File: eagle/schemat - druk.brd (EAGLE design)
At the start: 210 parts, among them IC1 MEGA8-AI, IC2 MEGA8-AI, IC3 MEGA8-AI, IC4 MEGA8-AI, IC5 MEGA8-AI, IC6 MEGA8-AI, Q1 N-MOSFET BSS138, Q10 N-MOSFET BSS138, Q11 N-MOSFET BSS138, Q12 N-MOSFET BSS138, Q2 N-MOSFET BSS138, Q3 N-MOSFET BSS138, Q4 N-MOSFET BSS138, Q5 N-MOSFET BSS138, Q6 N-MOSFET BSS138, Q7 N-MOSFET BSS138, Q8 N-MOSFET BSS138, Q9 N-MOSFET BSS138, U1 LCD-16X2SILK, U2 LCD-16X2SILK, U3 LCD-16X2SILK, U4 LCD-16X2SILK, U5 LCD-16X2SILK, U6 LCD-16X2SILK, Y1 16MHz, Y2 16MHz, Y3 16MHz, Y4 16MHz, Y5 16MHz, Y6 16MHz

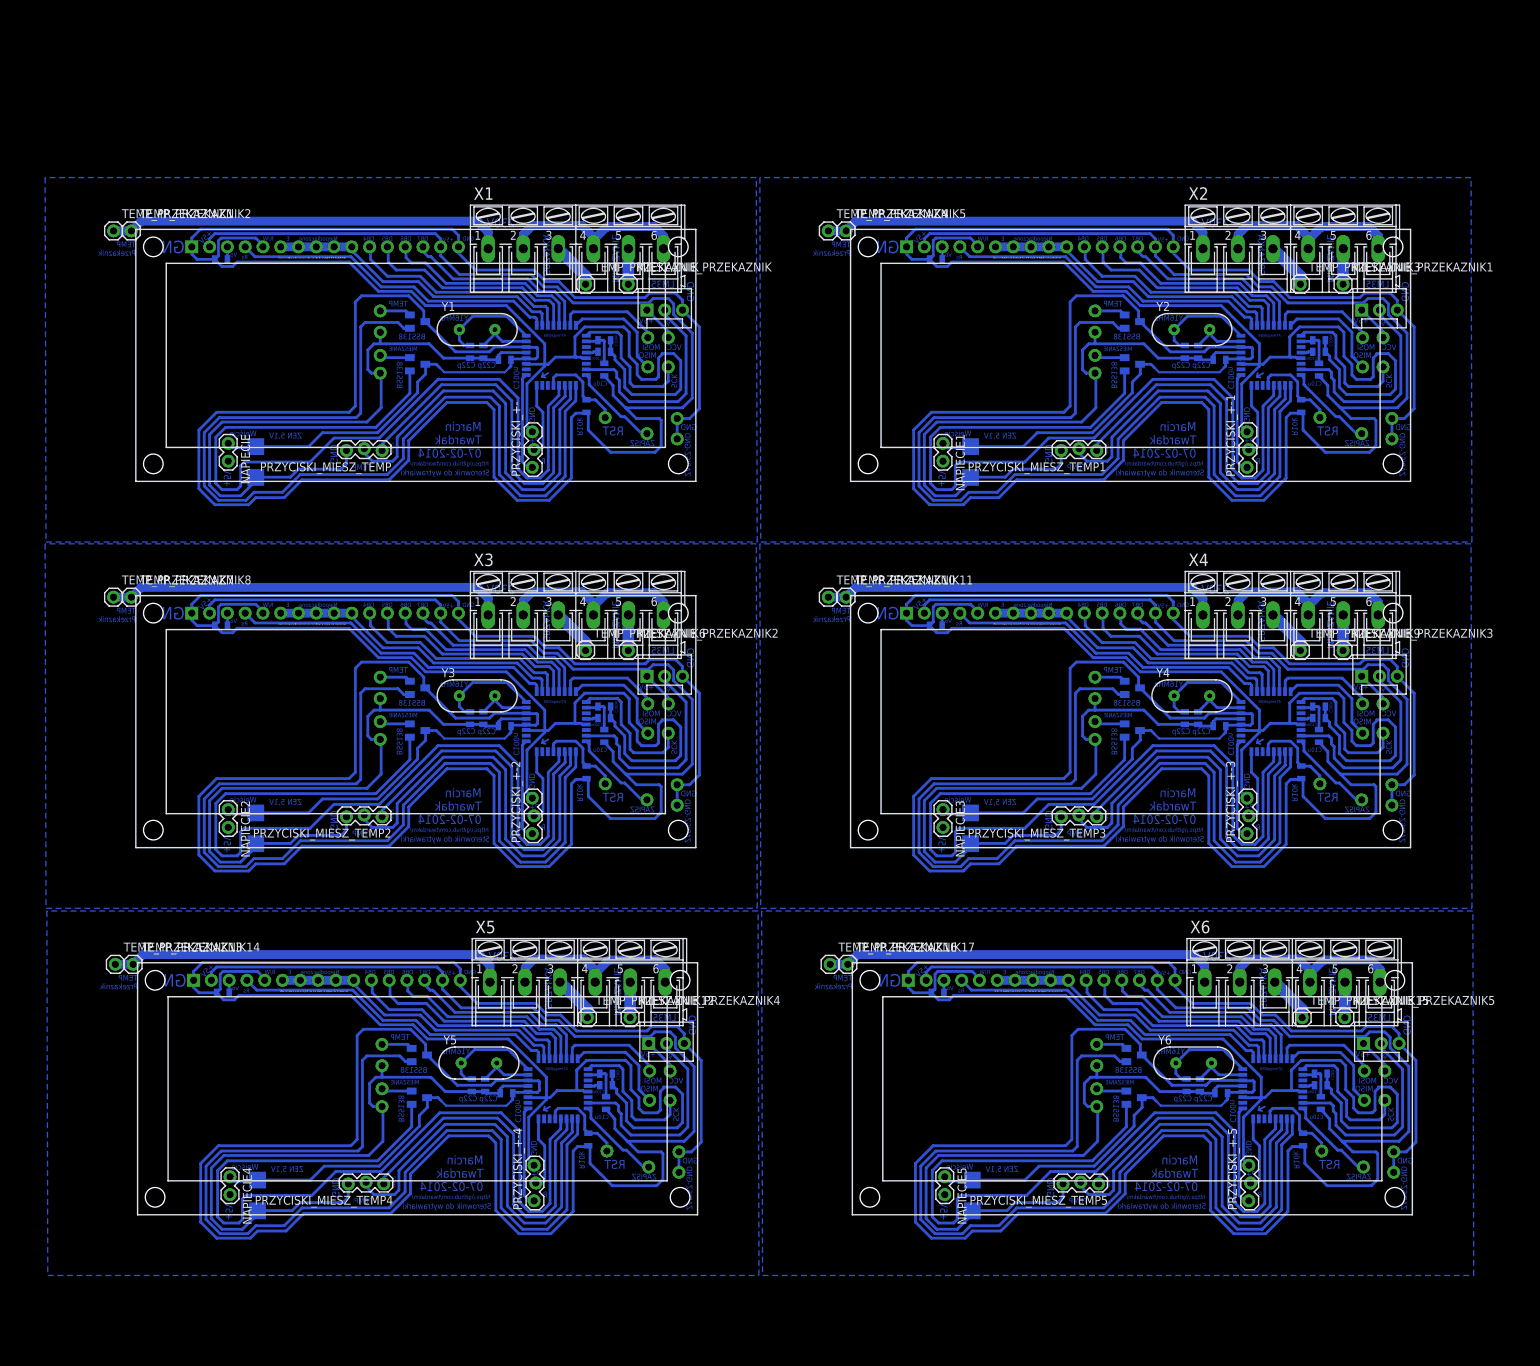
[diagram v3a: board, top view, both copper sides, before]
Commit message: Zmieniony schemat + zmiany w programie
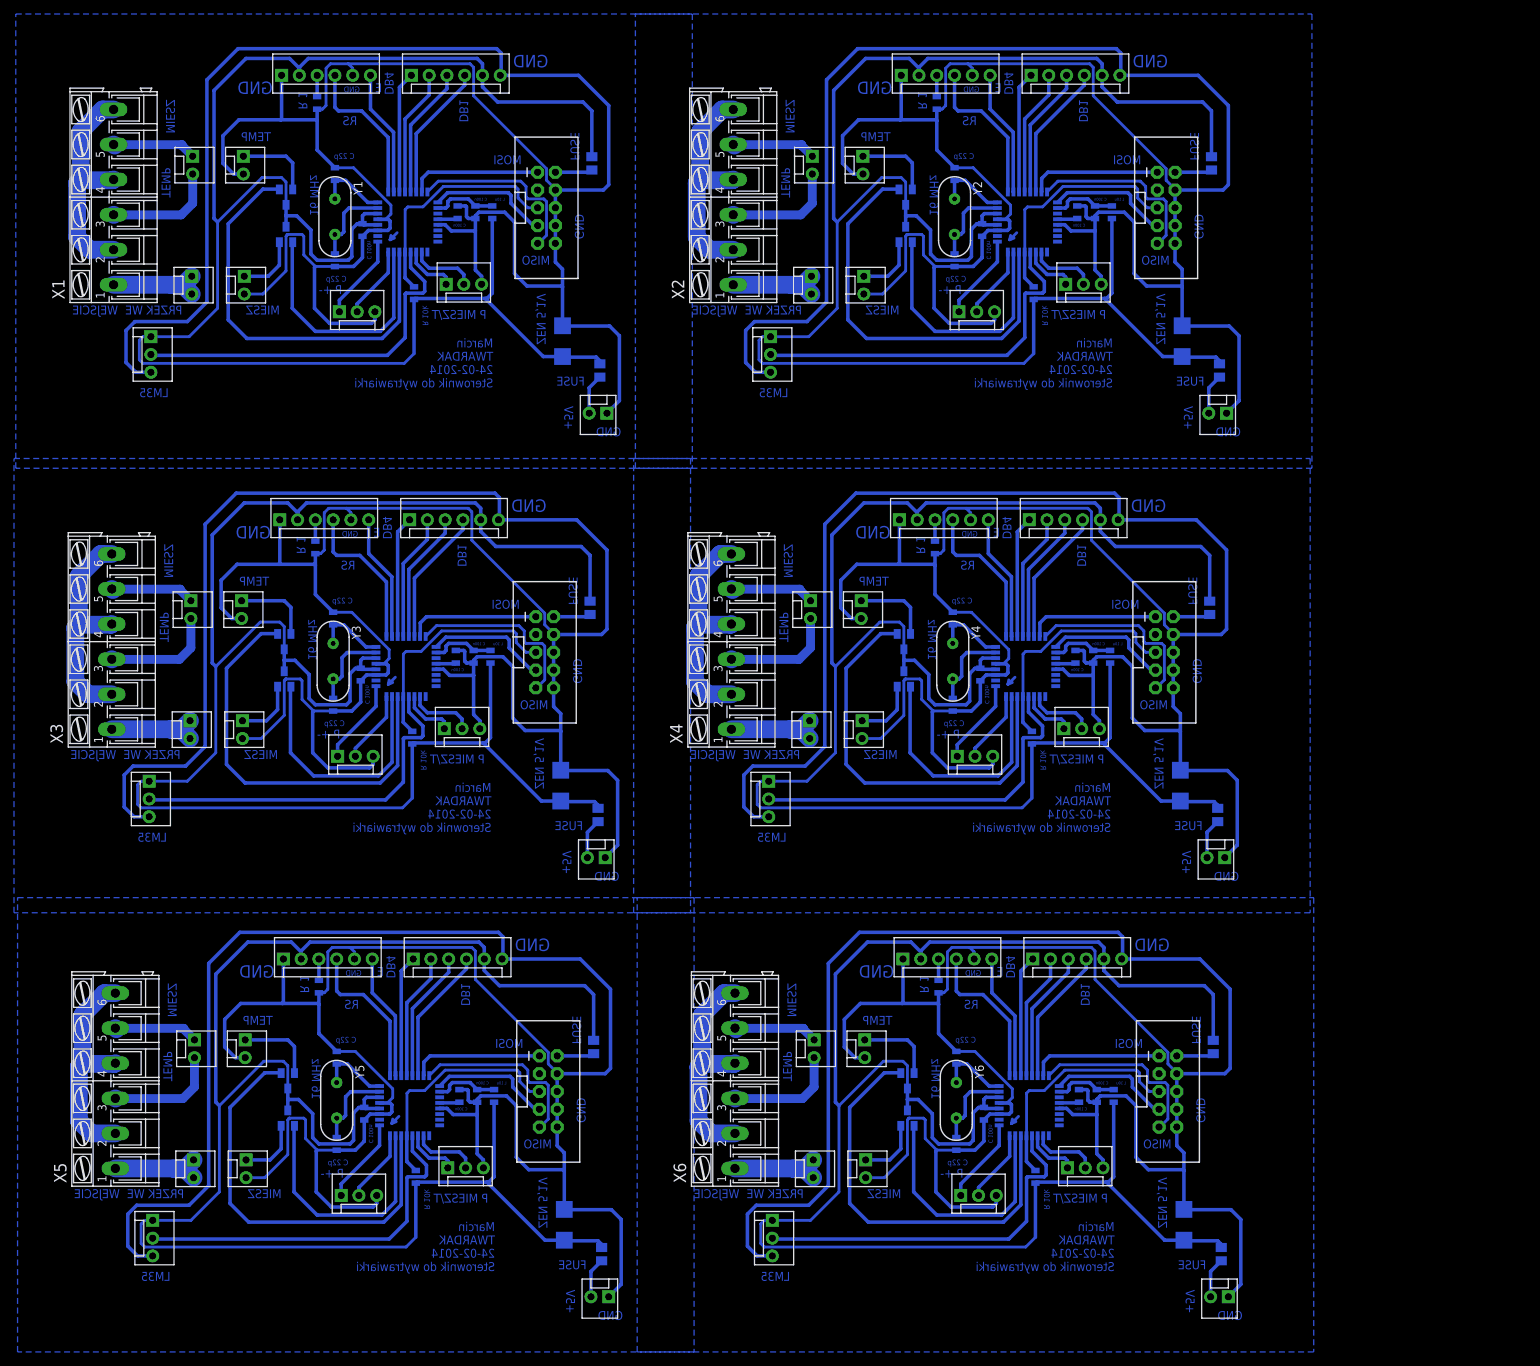
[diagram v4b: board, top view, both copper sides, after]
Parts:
- removed GND, GND1, GND2, GND3, GND4, GND5, MIESZANIE_GND, MIESZANIE_GND1, MIESZANIE_GND2, MIESZANIE_GND3, MIESZANIE_GND4, MIESZANIE_GND5, MISO, MISO1, MISO2, MISO3, MISO4, MISO5, MOSI, MOSI1, MOSI2, MOSI3, MOSI4, MOSI5, RESET, RESET1, RESET2, RESET3, RESET4, RESET5, SCK, SCK1, SCK2, SCK3, SCK4, SCK5, TEMP_GND, TEMP_GND1, TEMP_GND2, TEMP_GND3, TEMP_GND4, TEMP_GND5, VCC, VCC1, VCC2, VCC3, VCC4, VCC5, ZAPISZ, ZAPISZ1, ZAPISZ2, ZAPISZ3, ZAPISZ4, ZAPISZ5, ZAPISZ_GND, ZAPISZ_GND1, ZAPISZ_GND2, ZAPISZ_GND3, ZAPISZ_GND4, ZAPISZ_GND5: M01NOSILK-KIT, SparkFun-Connectors:1X01NS-KIT
- removed MIESZANIE_PRZEKAZNIK, MIESZANIE_PRZEKAZNIK1, MIESZANIE_PRZEKAZNIK2, MIESZANIE_PRZEKAZNIK3, MIESZANIE_PRZEKAZNIK4, MIESZANIE_PRZEKAZNIK5, TEMP_PRZEKAZNIK10, TEMP_PRZEKAZNIK11, TEMP_PRZEKAZNIK12, TEMP_PRZEKAZNIK13, TEMP_PRZEKAZNIK14, TEMP_PRZEKAZNIK15, TEMP_PRZEKAZNIK16, TEMP_PRZEKAZNIK17, TEMP_PRZEKAZNIK6, TEMP_PRZEKAZNIK7, TEMP_PRZEKAZNIK8, TEMP_PRZEKAZNIK9: M01PTH, SparkFun-Connectors:1X01
- removed U1, U2, U3, U4, U5, U6: LCD-16X2SILK, SparkFun-Displays:LCD-16X2
- added LCD1, LCD10, LCD11, LCD12, LCD2, LCD3, LCD4, LCD5, LCD6, LCD7, LCD8, LCD9: (no value), SparkFun-Connectors:MOLEX-1X6
- added PRZEKAZNIK_NAPIECIE, PRZEKAZNIK_NAPIECIE1, PRZEKAZNIK_NAPIECIE2, PRZEKAZNIK_NAPIECIE3, PRZEKAZNIK_NAPIECIE4, PRZEKAZNIK_NAPIECIE5: M02POLAR, SparkFun-Connectors:MOLEX-1X2
- added R13, R17, R21: 10k, SparkFun-Passives:0805
- added R14, R15, R18, R19, R22, R23: FUSE 500mA, resistor:M0805
- added R16, R20, R24: 1, SparkFun-Passives:0805
- added U$10, U$12, U$8: AVR_SPI_PROG2PTH2, SparkFun-Connectors:2X5-SHROUDED
- added U$11, U$7, U$9: ZENER 5V, SparkFun-DiscreteSemi:SMB-DIODE
- MIESZANIE, MIESZANIE1, MIESZANIE2, MIESZANIE3, MIESZANIE4, MIESZANIE5, TEMP, TEMP1, TEMP2, TEMP3, TEMP4, TEMP5: value M01NOSILK-KIT -> M02POLAR; device SparkFun-Connectors:1X01NS-KIT -> SparkFun-Connectors:MOLEX-1X2
- NAPIECIE, NAPIECIE1, NAPIECIE2, NAPIECIE3, NAPIECIE4, NAPIECIE5: value M02PTH -> M02POLAR; device SparkFun-Connectors:1X02 -> SparkFun-Connectors:MOLEX-1X2
- PRZYCISKI_+-, PRZYCISKI_+-1, PRZYCISKI_+-2, PRZYCISKI_+-3, PRZYCISKI_+-4, PRZYCISKI_+-5, PRZYCISKI_MIESZ_TEMP, PRZYCISKI_MIESZ_TEMP1, PRZYCISKI_MIESZ_TEMP2, PRZYCISKI_MIESZ_TEMP3, PRZYCISKI_MIESZ_TEMP4, PRZYCISKI_MIESZ_TEMP5: device SparkFun-Connectors:1X03_LOCK -> SparkFun-Connectors:MOLEX-1X3
- R10, R4, R6: value 1 -> FUSE 500mA; device SparkFun-Passives:0805 -> resistor:M0805
- R11, R3, R7: value 10k -> FUSE 500mA; device SparkFun-Passives:0805 -> resistor:M0805
- R2: value 1 -> 10k
- R5: value 10k -> 1
- TEMP_PRZEKAZNIK, TEMP_PRZEKAZNIK1, TEMP_PRZEKAZNIK2, TEMP_PRZEKAZNIK3, TEMP_PRZEKAZNIK4, TEMP_PRZEKAZNIK5: value M01PTH -> M02POLAR; device SparkFun-Connectors:1X01 -> SparkFun-Connectors:MOLEX-1X2
- U$2, U$4, U$6: value ZENER 5V -> AVR_SPI_PROG2PTH2; device SparkFun-DiscreteSemi:SMB-DIODE -> SparkFun-Connectors:2X5-SHROUDED
- moved U$3 149.5 mm to (155.2, 82.0), turned to 90 degrees
- moved R6 147.2 mm to (160.5, 77.9), turned to 90 degrees
- moved TEMP_PRZEKAZNIK4 146.8 mm to (14.1, -17.8), turned to 270 degrees
- moved R11 127.1 mm to (70.6, 43.9), turned to 90 degrees
- moved R2 116.2 mm to (134.0, 88.9), turned to 270 degrees
- moved TEMP_PRZEKAZNIK5 115.7 mm to (102.6, -17.8), turned to 270 degrees
- moved R12 109.3 mm to (31.4, 52.6), turned to 270 degrees
- moved R5 103.1 mm to (31.6, 116.1)
- moved TEMP_PRZEKAZNIK1 100.4 mm to (102.4, 108.5), turned to 270 degrees
- moved R3 100.3 mm to (72.0, 77.9), turned to 90 degrees
- moved U$6 98.8 mm to (64.1, 37.6), flipped to the top, turned to 0 degrees
- moved U$4 92.9 mm to (152.9, 101.1), flipped to the top, turned to 0 degrees
- moved LM5 88.2 mm to (96.6, -43.6), turned to 270 degrees
- moved R7 87.9 mm to (159.4, 107.4), turned to 90 degrees
- moved LM3 86.0 mm to (96.1, 19.2), turned to 270 degrees
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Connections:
- removed net N$13 (its old number): TEMP_PRZEKAZNIK.1, X1.3
- removed net N$17 (its old number): R4.1, U2.3
- removed net N$18 (its old number): TEMP_PRZEKAZNIK3.1, X2.3
- removed net N$27 (its old number): R6.1, U3.3
- removed net N$28 (its old number): TEMP_PRZEKAZNIK6.1, X3.3
- removed net N$29 (its old number): MIESZANIE_PRZEKAZNIK2.1, X3.5
- removed net N$37 (its old number): R8.1, U4.3
- removed net N$38 (its old number): TEMP_PRZEKAZNIK9.1, X4.3
- removed net N$39 (its old number): MIESZANIE_PRZEKAZNIK3.1, X4.5
- removed net N$48: TEMP_PRZEKAZNIK12.1, X5.3
- removed net N$49 (its old number): MIESZANIE_PRZEKAZNIK4.1, X5.5
- removed net N$9 (its old number): R2.1, U1.3
- removed net VCC: NAPIECIE.2
- removed net VCC1: NAPIECIE1.2
- removed net VCC2: NAPIECIE2.2
- removed net VCC3: NAPIECIE3.2
- removed net VCC4: NAPIECIE4.2
- removed net VCC5: NAPIECIE5.2
- new net N$10: TEMP_PRZEKAZNIK.2, X1.3
- new net N$11: R4.1, U$2.2
- new net N$16: LCD2.3, R5.1
- new net N$20: NAPIECIE1.2, R6.1
- new net N$21: TEMP_PRZEKAZNIK1.2, X2.3
- new net N$22: R7.1, U$4.2
- new net N$23: LCD4.3, R8.1
- new net N$31: TEMP_PRZEKAZNIK2.1, X3.5
- new net N$32: NAPIECIE2.2, R10.1
- new net N$33: TEMP_PRZEKAZNIK2.2, X3.3
- new net N$34: R11.1, U$6.2
- new net N$35: LCD6.3, R12.1
- new net N$43: TEMP_PRZEKAZNIK3.1, X4.5
- new net N$44: NAPIECIE3.2, R14.1
- new net N$45: TEMP_PRZEKAZNIK3.2, X4.3
- new net N$46: R15.1, U$8.2
- new net N$55: TEMP_PRZEKAZNIK4.1, X5.5
- new net N$56: NAPIECIE4.2, R18.1
- new net N$67: TEMP_PRZEKAZNIK5.1, X6.5
- new net N$68: NAPIECIE5.2, R22.1
- new net N$69: TEMP_PRZEKAZNIK5.2, X6.3
- new net N$70: R23.1, U$12.2
- new net N$71: LCD12.3, R24.1
- new net N$8: NAPIECIE.2, R3.1
- net +5V: now also LCD1.5, LCD2.2, R3.2, R4.2; no longer NAPIECIE.1, U1.15, U1.2, VCC.1
- net +5V1: now also LCD3.5, LCD4.2, R2.2, R6.2, R7.2, U$3.C; no longer NAPIECIE1.1, R3.2, U$2.C, U2.15, U2.2, VCC1.1
- net +5V2: now also LCD5.5, LCD6.2, R10.2, R11.2, R9.2, U$5.C; no longer NAPIECIE2.1, R5.2, U$3.C, U3.15, U3.2, VCC2.1
- net +5V3: now also LCD7.5, LCD8.2, R13.2, R14.2, R15.2, U$7.C; no longer NAPIECIE3.1, R7.2, U$4.C, U4.15, U4.2, VCC3.1
- net +5V4: now also LCD10.2, LCD9.5, R17.2, R18.2, R19.2, U$9.C; no longer NAPIECIE4.1, R9.2, U$5.C, U5.15, U5.2, VCC4.1
- net +5V5: now also LCD11.5, LCD12.2, R21.2, R22.2, R23.2, U$11.C; no longer NAPIECIE5.1, R11.2, U$6.C, U6.15, U6.2, VCC5.1
- net DB1: now also LCD3.1; no longer U2.11
- net DB10: now also LCD5.2; no longer U3.12
- net DB11: now also LCD5.3; no longer U3.13
- net DB12: now also LCD5.4; no longer U3.14
- net DB13: now also LCD7.1; no longer U4.11
- net DB14: now also LCD7.2; no longer U4.12
- net DB15: now also LCD7.3; no longer U4.13
- net DB16: now also LCD7.4; no longer U4.14
- net DB17: now also LCD9.1; no longer U5.11
- net DB18: now also LCD9.2; no longer U5.12
- net DB19: now also LCD9.3; no longer U5.13
- net DB2: now also LCD3.2; no longer U2.12
- net DB20: now also LCD9.4; no longer U5.14
- net DB21: now also LCD11.1; no longer U6.11
- net DB22: now also LCD11.2; no longer U6.12
- net DB23: now also LCD11.3; no longer U6.13
- net DB24: now also LCD11.4; no longer U6.14
- net DB3: now also LCD3.3; no longer U2.13
- net DB4: now also LCD1.1; no longer U1.11
- net DB5: now also LCD1.2; no longer U1.12
- net DB6: now also LCD1.3; no longer U1.13
- net DB7: now also LCD1.4; no longer U1.14
- net DB8: now also LCD3.4; no longer U2.14
- net DB9: now also LCD5.1; no longer U3.11
- net E: now also LCD2.6; no longer U1.6
- net E1: now also LCD4.6; no longer U2.6
- net E2: now also LCD6.6; no longer U3.6
- net E3: now also LCD8.6; no longer U4.6
- net E4: now also LCD10.6; no longer U5.6
- net E5: now also LCD12.6; no longer U6.6
- net GND: now also LCD1.6, LCD2.1, LCD2.5, MIESZANIE.2, NAPIECIE.1, R5.2, TEMP.2, U$2.10, U$2.4, U$2.6, U$2.8; no longer GND.1, MIESZANIE_GND.1, R2.2, TEMP_GND.1, U1.1, U1.16, U1.5, ZAPISZ_GND.1
- net GND1: now also LCD3.6, LCD4.1, LCD4.5, MIESZANIE1.2, NAPIECIE1.1, R8.2, TEMP1.2, U$3.A, U$4.10, U$4.4, U$4.6, U$4.8; no longer GND1.1, MIESZANIE_GND1.1, R4.2, TEMP_GND1.1, U$2.A, U2.1, U2.16, U2.5, ZAPISZ_GND1.1
- net GND2: now also LCD5.6, LCD6.1, LCD6.5, MIESZANIE2.2, NAPIECIE2.1, R12.2, TEMP2.2, U$5.A, U$6.10, U$6.4, U$6.6, U$6.8; no longer GND2.1, MIESZANIE_GND2.1, R6.2, TEMP_GND2.1, U$3.A, U3.1, U3.16, U3.5, ZAPISZ_GND2.1
- net GND3: now also LCD7.6, LCD8.1, LCD8.5, MIESZANIE3.2, NAPIECIE3.1, R16.2, TEMP3.2, U$7.A, U$8.10, U$8.4, U$8.6, U$8.8; no longer GND3.1, MIESZANIE_GND3.1, R8.2, TEMP_GND3.1, U$4.A, U4.1, U4.16, U4.5, ZAPISZ_GND3.1
- net GND4: now also LCD10.1, LCD10.5, LCD9.6, MIESZANIE4.2, NAPIECIE4.1, R20.2, TEMP4.2, U$10.10, U$10.4, U$10.6, U$10.8, U$9.A; no longer GND4.1, MIESZANIE_GND4.1, R10.2, TEMP_GND4.1, U$5.A, U5.1, U5.16, U5.5, ZAPISZ_GND4.1
- net GND5: now also LCD11.6, LCD12.1, LCD12.5, MIESZANIE5.2, NAPIECIE5.1, R24.2, TEMP5.2, U$11.A, U$12.10, U$12.4, U$12.6, U$12.8; no longer GND5.1, MIESZANIE_GND5.1, R12.2, TEMP_GND5.1, U$6.A, U6.1, U6.16, U6.5, ZAPISZ_GND5.1
- net LM1: now also IC2.28; no longer IC2.23
- net LM2: now also IC3.28; no longer IC3.23
- net LM3: now also IC4.28; no longer IC4.23
- net LM35: now also IC1.28; no longer IC1.23
- net LM4: now also IC5.28; no longer IC5.23
- net LM5: now also IC6.28; no longer IC6.23
- net MIESZANIE: now also IC1.31; no longer IC1.28
- net MIESZANIE1: now also IC2.31; no longer IC2.28
- net MIESZANIE2: now also IC3.31; no longer IC3.28
- net MIESZANIE3: now also IC4.31; no longer IC4.28
- net MIESZANIE4: now also IC5.31; no longer IC5.28
- net MIESZANIE5: now also IC6.31; no longer IC6.28
- net MISO: now also U$2.9; no longer MISO.1
- net MISO1: now also U$4.9; no longer MISO1.1
- net MISO2: now also U$6.9; no longer MISO2.1
- net MISO3: now also U$8.9; no longer MISO3.1
- net MISO4: now also U$10.9; no longer MISO4.1
- net MISO5: now also U$12.9; no longer MISO5.1
- net MOSI: now also U$2.1; no longer MOSI.1
- net MOSI1: now also U$4.1; no longer MOSI1.1
- net MOSI2: now also U$6.1; no longer MOSI2.1
- net MOSI3: now also U$8.1; no longer MOSI3.1
- net MOSI4: now also U$10.1; no longer MOSI4.1
- net MOSI5: now also U$12.1; no longer MOSI5.1
- net N$14: now also TEMP_PRZEKAZNIK.1; no longer MIESZANIE_PRZEKAZNIK.1
- net N$19: now also TEMP_PRZEKAZNIK1.1; no longer MIESZANIE_PRZEKAZNIK1.1
- net N$47: now also LCD8.3, R16.1; no longer R10.1, U5.3
- net N$57: now also TEMP_PRZEKAZNIK4.2, X5.3; no longer R12.1, U6.3
- net N$58: now also R19.1, U$10.2; no longer TEMP_PRZEKAZNIK15.1, X6.3
- net N$59: now also LCD10.3, R20.1; no longer MIESZANIE_PRZEKAZNIK5.1, X6.5
- net RESET: now also U$2.5; no longer RESET.1
- net RESET1: now also R2.1, U$4.5; no longer R3.1, RESET1.1
- net RESET2: now also R9.1, U$6.5; no longer R5.1, RESET2.1
- net RESET3: now also R13.1, U$8.5; no longer R7.1, RESET3.1
- net RESET4: now also R17.1, U$10.5; no longer R9.1, RESET4.1
- net RESET5: now also R21.1, U$12.5; no longer R11.1, RESET5.1
- net RS: now also LCD2.4; no longer U1.4
- net RS1: now also LCD4.4; no longer U2.4
- net RS2: now also LCD6.4; no longer U3.4
- net RS3: now also LCD8.4; no longer U4.4
- net RS4: now also LCD10.4; no longer U5.4
- net RS5: now also LCD12.4; no longer U6.4
- net SCK: now also U$2.7; no longer SCK.1
- net SCK1: now also U$4.7; no longer SCK1.1
- net SCK2: now also U$6.7; no longer SCK2.1
- net SCK3: now also U$8.7; no longer SCK3.1
- net SCK4: now also U$10.7; no longer SCK4.1
- net SCK5: now also U$12.7; no longer SCK5.1
- net TEMP: now also IC1.30; no longer IC1.25
- net TEMP1: now also IC2.30; no longer IC2.25
- net TEMP2: now also IC3.30; no longer IC3.25
- net TEMP3: now also IC4.30; no longer IC4.25
- net TEMP4: now also IC5.30; no longer IC5.25
- net TEMP5: now also IC6.30; no longer IC6.25
- net VDD: now also PRZEKAZNIK_NAPIECIE.1, PRZEKAZNIK_NAPIECIE.2; no longer TEMP_PRZEKAZNIK1.1, TEMP_PRZEKAZNIK2.1
- net VDD1: now also PRZEKAZNIK_NAPIECIE1.1, PRZEKAZNIK_NAPIECIE1.2; no longer TEMP_PRZEKAZNIK4.1, TEMP_PRZEKAZNIK5.1
- net VDD2: now also PRZEKAZNIK_NAPIECIE2.1, PRZEKAZNIK_NAPIECIE2.2; no longer TEMP_PRZEKAZNIK7.1, TEMP_PRZEKAZNIK8.1
- net VDD3: now also PRZEKAZNIK_NAPIECIE3.1, PRZEKAZNIK_NAPIECIE3.2; no longer TEMP_PRZEKAZNIK10.1, TEMP_PRZEKAZNIK11.1
- net VDD4: now also PRZEKAZNIK_NAPIECIE4.1, PRZEKAZNIK_NAPIECIE4.2; no longer TEMP_PRZEKAZNIK13.1, TEMP_PRZEKAZNIK14.1
- net VDD5: now also PRZEKAZNIK_NAPIECIE5.1, PRZEKAZNIK_NAPIECIE5.2; no longer TEMP_PRZEKAZNIK16.1, TEMP_PRZEKAZNIK17.1
- net ZAPISZ: no longer ZAPISZ.1
- net ZAPISZ1: no longer ZAPISZ1.1
- net ZAPISZ2: no longer ZAPISZ2.1
- net ZAPISZ3: no longer ZAPISZ3.1
- net ZAPISZ4: no longer ZAPISZ4.1
- net ZAPISZ5: no longer ZAPISZ5.1
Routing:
- net +5V5: track 352.9 -> 253.2 mm
- net +5V2: track 352.9 -> 253.2 mm
- net +5V4: track 352.9 -> 253.2 mm
- net +5V: track 352.9 -> 253.2 mm
- net +5V3: track 352.9 -> 253.2 mm
- net +5V1: track 352.9 -> 253.2 mm
- net MIESZANIE4: track 121.2 -> 35.5 mm
- net MIESZANIE3: track 121.2 -> 35.5 mm
- net MIESZANIE2: track 121.2 -> 35.5 mm
- net MIESZANIE1: track 121.2 -> 35.5 mm
- net MIESZANIE: track 121.2 -> 35.5 mm
- net MIESZANIE5: track 121.2 -> 35.5 mm
- net TEMP4: track 137.6 -> 59.5 mm
- net TEMP1: track 137.6 -> 59.5 mm
- net TEMP5: track 137.6 -> 59.5 mm
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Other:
- board text added: "16 MHz"
- board text added: "C 100n"
- board text added: "C 22p"
- board text added: "DB1"
- board text added: "FUSE"
- board text added: "L 10u"
- board text added: "Marcin TWARDAK 24-02-2014 Sterownik do wytrawiarki"
- board text added: "P +-"
- board text added: "P MIESZ/T"
- board text added: "PRZEK WE"
- board text added: "R 1"
- board text added: "R 10k"
- board text added: "RS"
- board text added: "WEJSCIE"
- board text removed: "ADC"
- board text removed: "ATmega8/88"
- board text removed: "BSS138"
- board text removed: "C100n"
- board text removed: "C10u"
- board text removed: "C22p"
- board text removed: "DB5"
- board text removed: "DB6"
- board text removed: "DB7"
- board text removed: "GRZAŁKA"
- board text removed: "MIESZANIE"
- board text removed: "Marcin Twardak 07-02-2014"
- board text removed: "Niepodłączone"
- board text removed: "Olać te otwory do ktorych nic nie idzie, w ogóle nie wywiercać"
- board text removed: "P+"
- board text removed: "P-"
- board text removed: "R/W"
- board text removed: "R10k"
- board text removed: "RST"
- board text removed: "Rs"
- board text removed: "SCK"
- board text removed: "Sterownik do wytrawiarki"
- board text removed: "TEMP Przekaznik"
- board text removed: "VCC"
- board text removed: "Vo"
- board text removed: "Wejście"
- board text removed: "Y16MHz"
- board text removed: "ZAPISZ"
- board text removed: "ZAPISZ-GND"
- board text removed: "https://github.com/twardakm/"
- board text removed: "~230V"
